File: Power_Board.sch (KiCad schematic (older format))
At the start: 7 parts, among them J1 Input Power (12 V), J2 Output Power (5V), SW1 SW_SPST

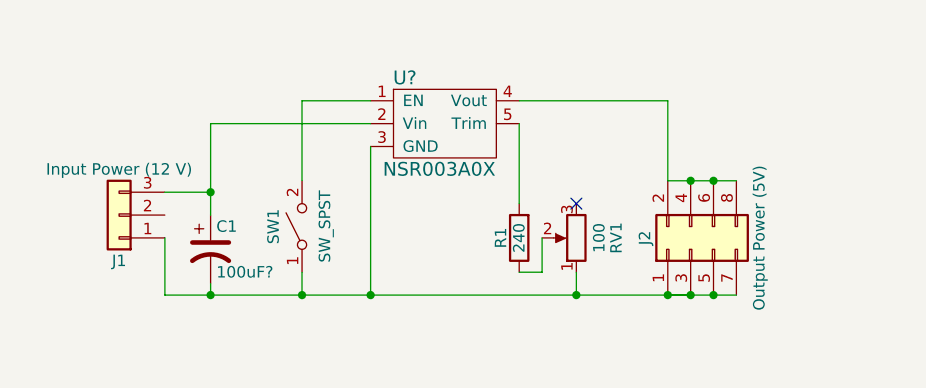
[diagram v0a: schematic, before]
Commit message: Updated design, added backplane
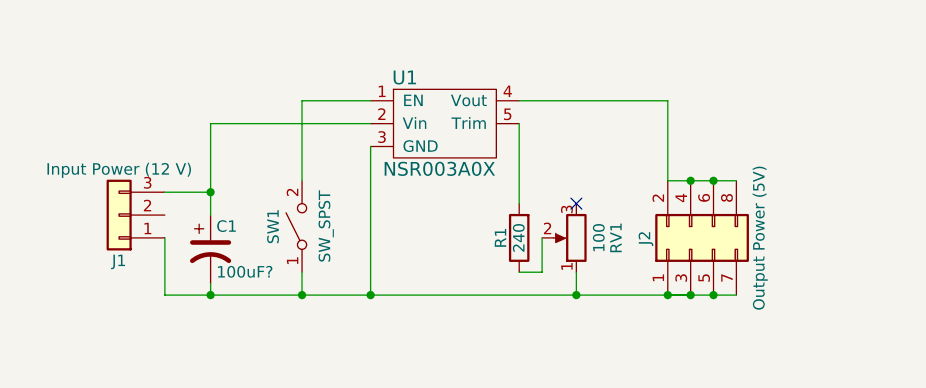
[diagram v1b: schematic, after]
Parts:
- C1: footprint (none) -> Capacitors_THT:CP_Radial_D12.5mm_P5.00mm
- J1: footprint (none) -> Pin_Headers:Pin_Header_Straight_1x03_Pitch1.00mm
- J2: footprint (none) -> Pin_Headers:Pin_Header_Straight_2x04_Pitch1.00mm
- R1: footprint (none) -> Resistors_THT:R_Axial_DIN0207_L6.3mm_D2.5mm_P10.16mm_Horizontal
- RV1: footprint (none) -> Potentiometers:Potentiometer_Trimmer_Bourns_3006P
- SW1: footprint (none) -> Buttons_Switches_THT:SW_CuK_OS102011MA1QN1_SPDT_Angled
- U1: renamed from U?; footprint (none) -> NSR003A0X:NSR003A0X
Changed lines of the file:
@@
 LIBS:valves
 LIBS:nsr003a0x
+LIBS:OS_Switches_2
+LIBS:Power_Board-cache
 EELAYER 25 0
 EELAYER END
@@
 F 0 "R1" V 5880 3000 50  0000 C CNN
 F 1 "240" V 5800 3000 50  0000 C CNN
-F 2 "" V 5730 3000 50  0001 C CNN
+F 2 "Resistors_THT:R_Axial_DIN0207_L6.3mm_D2.5mm_P10.16mm_Horizontal" V 5730 3000 50  0001 C CNN
 F 3 "" H 5800 3000 50  0001 C CNN
 	1    5800 3000
@@
 F 0 "J1" H 4050 3100 50  0000 C CNN
 F 1 "Input Power (12 V)" H 4050 2700 50  0000 C CNN
-F 2 "" H 4050 2900 50  0001 C CNN
+F 2 "Pin_Headers:Pin_Header_Straight_1x03_Pitch1.00mm" H 4050 2900 50  0001 C CNN
 F 3 "" H 4050 2900 50  0001 C CNN
 	1    4050 2900
@@
 F 0 "J2" H 6600 3250 50  0000 C CNN
 F 1 "Output Power (5V)" H 6600 2750 50  0000 C CNN
-F 2 "" H 6550 3050 50  0001 C CNN
+F 2 "Pin_Headers:Pin_Header_Straight_2x04_Pitch1.00mm" H 6550 3050 50  0001 C CNN
 F 3 "" H 6550 3050 50  0001 C CNN
 	1    6550 3050
@@
 F 0 "RV1" V 5875 3000 50  0000 C CNN
 F 1 "100" V 5950 3000 50  0000 C CNN
-F 2 "" H 6050 3000 50  0001 C CNN
+F 2 "Potentiometers:Potentiometer_Trimmer_Bourns_3006P" H 6050 3000 50  0001 C CNN
 F 3 "" H 6050 3000 50  0001 C CNN
 	1    6050 3000
@@
 	5900 3150 5800 3150
 $Comp
-L NSR003A0X U?
+L NSR003A0X U1
 U 1 1 5A8DED87
 P 5450 2700
-F 0 "U?" H 5300 3100 60  0000 C CNN
+F 0 "U1" H 5300 3100 60  0000 C CNN
 F 1 "NSR003A0X" H 5450 2700 60  0000 C CNN
-F 2 "" H 5450 2700 60  0001 C CNN
+F 2 "NSR003A0X:NSR003A0X" H 5450 2700 60  0001 C CNN
 F 3 "" H 5450 2700 60  0001 C CNN
 	1    5450 2700
@@
 F 0 "C1" H 4475 3150 50  0000 L CNN
 F 1 "100uF?" H 4475 2950 50  0000 L CNN
-F 2 "" H 4450 3050 50  0001 C CNN
+F 2 "Capacitors_THT:CP_Radial_D12.5mm_P5.00mm" H 4450 3050 50  0001 C CNN
 F 3 "" H 4450 3050 50  0001 C CNN
 	1    4450 3050
@@
 F 0 "SW1" H 4850 3075 50  0000 C CNN
 F 1 "SW_SPST" H 4850 2850 50  0000 C CNN
-F 2 "" H 4850 2950 50  0001 C CNN
+F 2 "Buttons_Switches_THT:SW_CuK_OS102011MA1QN1_SPDT_Angled" H 4850 2950 50  0001 C CNN
 F 3 "" H 4850 2950 50  0001 C CNN
 	1    4850 2950

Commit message: Updated to version 2, corrected footprints
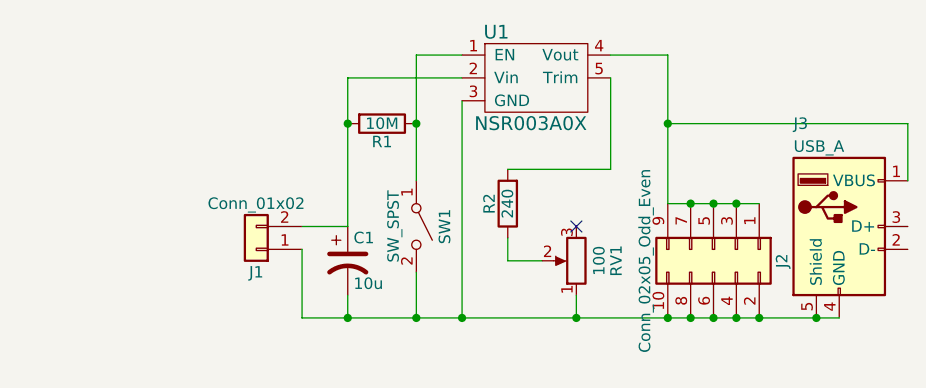
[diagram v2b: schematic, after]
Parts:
- removed J1: Input Power (12 V), Pin_Headers:Pin_Header_Straight_1x03_Pitch1.00mm, symbol Conn_01x03
- removed J2: Output Power (5V), Pin_Headers:Pin_Header_Straight_2x04_Pitch1.00mm, symbol Conn_02x04_Odd_Even
- added J1: Conn_01x02, symbol Conn_01x02
- added J2: Conn_02x05_Odd_Even, symbol Conn_02x05_Odd_Even
- added J3: USB_A, symbol USB_A
- added R2: 240, symbol R
- C1: value 100uF? -> 10u; footprint Capacitors_THT:CP_Radial_D12.5mm_P5.00mm -> (none)
- R1: value 240 -> 10M; footprint Resistors_THT:R_Axial_DIN0207_L6.3mm_D2.5mm_P10.16mm_Horizontal -> (none)
- RV1: footprint Potentiometers:Potentiometer_Trimmer_Bourns_3006P -> (none)
- SW1: footprint Buttons_Switches_THT:SW_CuK_OS102011MA1QN1_SPDT_Angled -> (none)
- U1: footprint NSR003A0X:NSR003A0X -> (none)
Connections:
- net at RV1.2: now also R2.1; no longer R1.1
- net at R1.2: now also C1.1, U1.2 (Vin), J1.2 (Pin_2); no longer U1.5 (Trim)
- net at C1.2, RV1.1, U1.3 (GND): now also SW1.2 (B), J1.1 (Pin_1), J2.10 (Pin_10), J2.2 (Pin_2), J2.4 (Pin_4), J2.6 (Pin_6), J2.8 (Pin_8), J3.4 (GND), J3.5 (Shield); no longer SW1.1 (A)
- net at U1.4 (Vout): now also J2.1 (Pin_1), J2.3 (Pin_3), J2.5 (Pin_5), J2.7 (Pin_7), J2.9 (Pin_9), J3.1 (VBUS)
- net at U1.1 (EN): now also R1.1, SW1.1 (A); no longer SW1.2 (B)
- new net: R2.2, U1.5 (Trim)
